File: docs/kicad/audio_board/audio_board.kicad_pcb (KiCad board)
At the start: 2 copper layers, 13 parts, among them J1 RPI_ILI9488, J2 rpi_connector, J3 T40 Power, J4 teensy Controller, J6 T4 Serial, J7 Host USB, U1 myTeensy4.0_mod

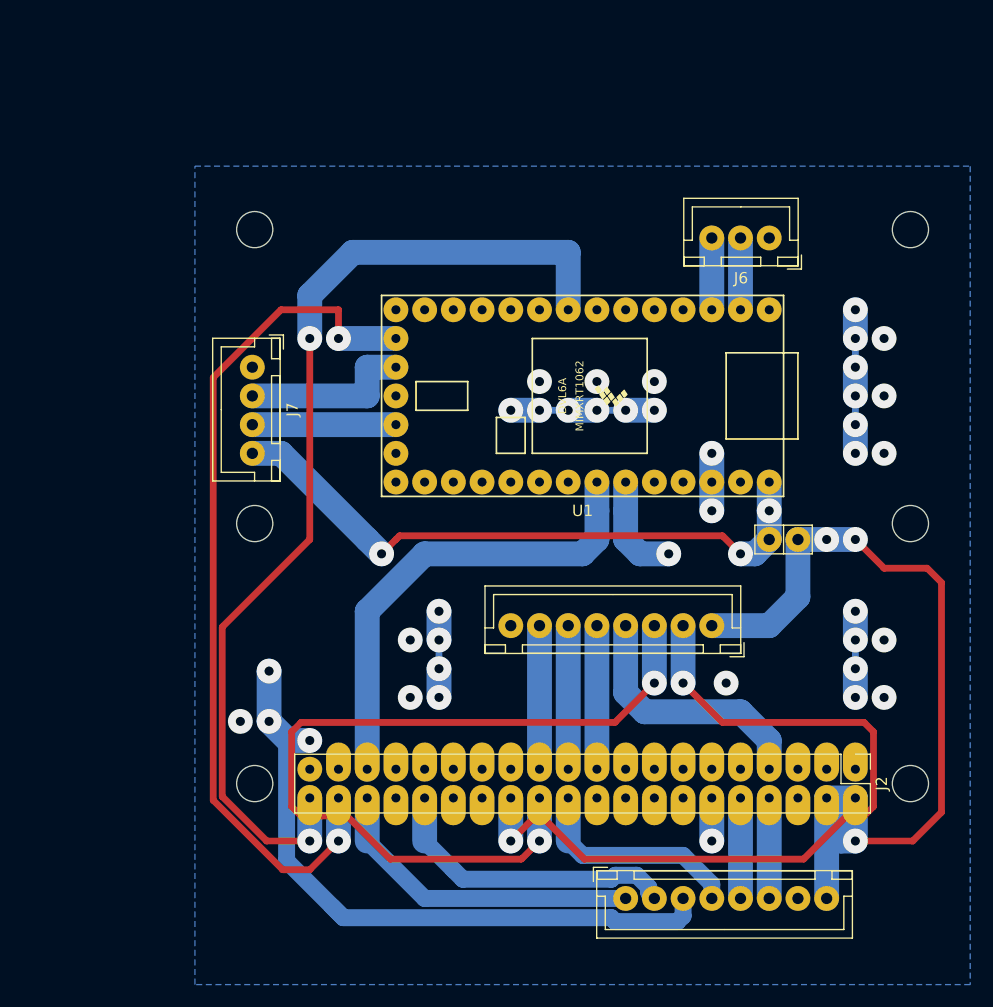
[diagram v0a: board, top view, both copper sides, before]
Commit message: added audio_breadboard, touched the audio_board design
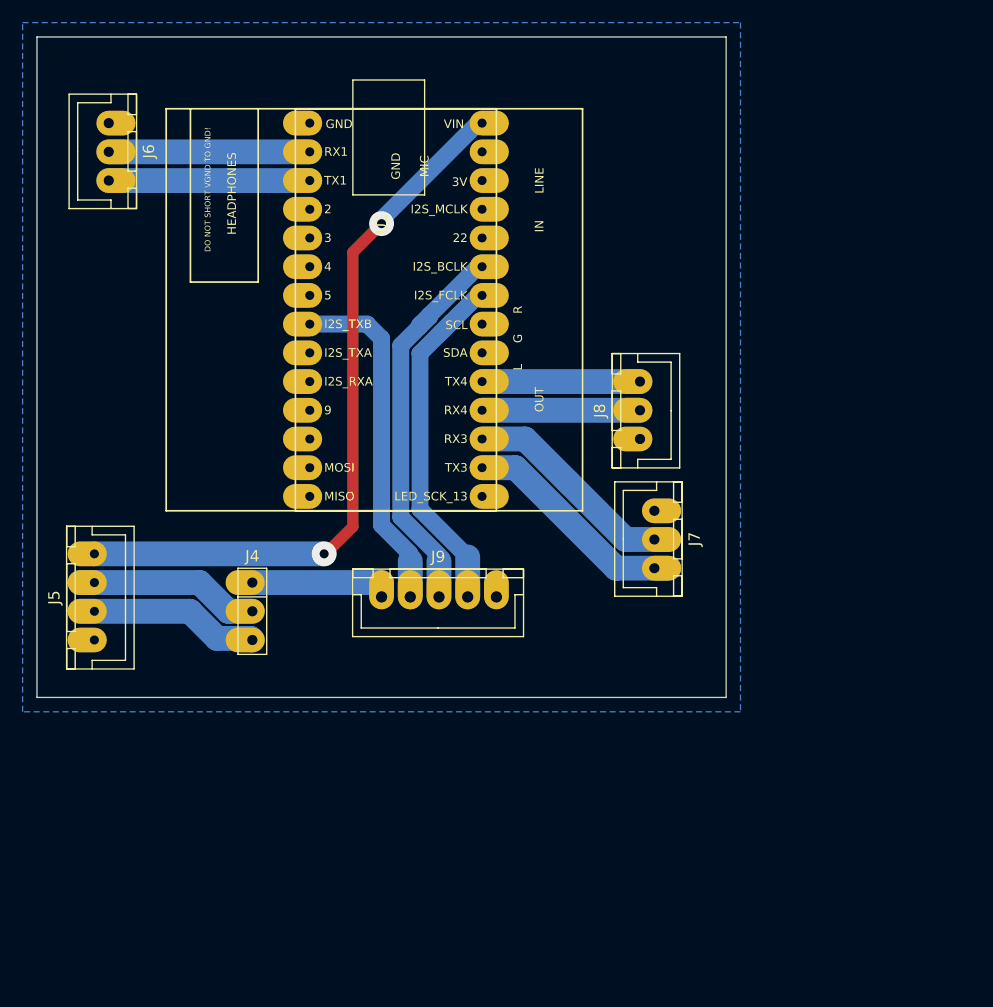
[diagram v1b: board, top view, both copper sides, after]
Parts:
- removed J1: RPI_ILI9488, 0_my_footprints:myJSTx08
- removed J2: rpi_connector, 0_my_footprints:myRpiConnector_bottom
- removed J3: T40 Power, 0_my_footprints:myPinHeader_1x02
- removed REF** (x6): myMountingHole_3.2mm_M3, 0_my_footprints:myMountingHole_3.2mm_M3
- added J5: Host USB, 0_my_footprints2:JST4, F.Cu at (36.8, 83.8)
- added J8: T4 Serial4, 0_my_footprints2:JST3, F.Cu at (85.1, 66.0)
- added J9: rPi I2S, 0_my_footprints2:JST5, F.Cu at (62.2, 80.0)
- J4: value teensy Controller -> T4 bottom; footprint 0_my_footprints:myJSTx08 -> 0_my_footprints2:pinHeader1x3
- J6: value T4 Serial -> T4 Serial1; footprint 0_my_footprints:myJSTx03 -> 0_my_footprints2:JST3
- J7: value Host USB -> T4 Serial3; footprint 0_my_footprints:myJSTx04 -> 0_my_footprints2:JST3
- U1: value myTeensy4.0_mod -> teensyAudioRevD; footprint 0_my_teensy:myTeensy40_mod -> 0_my_teensy:audioShieldRevD
- moved J6 59.3 mm to (38.1, 38.1), turned to 270 degrees
- moved U1 43.9 mm to (55.9, 38.1), turned to 270 degrees
- moved J4 43.3 mm to (50.8, 78.7)
- moved J7 37.8 mm to (86.4, 72.4)
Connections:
- net Net-(U1-Pad12) renamed AUDIO_SD_CS!
- J4 pad 1: RPI_I2S_TX_ACTIVE -> T40_I2S_RXB
- J4 pad 2: RPI_I2S_RX_ACTIVE -> HOST_D-
- J4 pad 3: RPI_RUN -> HOST_D+
- J7 pad 2: HOST_D+ -> T40_RX3
- J7 pad 3: HOST_D- -> T40_TX3
- U1 pad 16: Net-(U1-Pad16) -> T40_TX3
- U1 pad 17: Net-(U1-Pad17) -> T40_RX3
- U1 pad 18: Net-(U1-Pad18) -> T40_RX4
- U1 pad 19: Net-(U1-Pad19) -> T40_TX4
- U1 pad 22: LRCLK1 -> I2S_FCLK
- U1 pad 23: BCLK1 -> I2S_BCLK
- U1 pad 8: I2S_RX1B -> T40_I2S_TXB
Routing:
- net I2S_RX1B: track 90.2 -> 0.00 mm, vias 2 -> 0
- net I2S_TX1B: track 77.1 -> 0.00 mm, vias 2 -> 0
- net RPI_5V: track 76.1 -> 0.00 mm, vias 3 -> 0
- net RPI_LED_CS: track 73.9 -> 0.00 mm, vias 2 -> 0
- net RPI_TOUCH_CS: track 70.6 -> 0.00 mm, vias 2 -> 0
- net RPI_RUN: track 59.9 -> 0.00 mm, vias 3 -> 0
- net (no net): track 50.8 -> 0.00 mm, vias 21 -> 0
- net LRCLK1: track 42.0 -> 0.00 mm
- net I2S_BCLK: track 0.00 -> 34.7 mm
- net I2S_FCLK: track 0.00 -> 32.4 mm
- net T40_I2S_TXB: track 0.00 -> 31.4 mm
- net RPI_I2S_TX_ACTIVE: track 28.8 -> 0.00 mm
- net RPI_I2S_RX_ACTIVE: track 26.8 -> 0.00 mm
- net RPI_CD: track 22.9 -> 0.00 mm
- net T40_RX3: track 0.00 -> 20.2 mm
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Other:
- board outline added: 61 x 58.4 mm
- board text removed: "Horzontally, it is 29mm from the center of the holes to the center of the connector."
- board text removed: "The vertical center of the rPi holes line up with the center of the rPi connector"
- board text removed: "There are 1.27 + 9*2.54 = 24.13 mm from the center of the connector to the leftmost pin"
- board text removed: "Therefore, the left most hole is 29-24.13 =4.87mm from the left most pin to the center of the hole"
- board text removed: "rpi3B+ run pin"
- board text removed: "rpiZero Run Pin"
